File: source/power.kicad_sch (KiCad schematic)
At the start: 105 parts, among them Q1 MMBT5401, Q10 MMBT5401, Q11 CSD19536KCS, Q12 CSD19536KCS, Q2 MMBT5401, Q3 CSD19536KCS, Q4 CSD19536KCS, Q5 MMBT5401, Q6 MMBT5401, Q7 CSD19536KCS, Q8 CSD19536KCS, Q9 MMBT5401, U10 MS8311, U8 MS8311, U9 MS8311

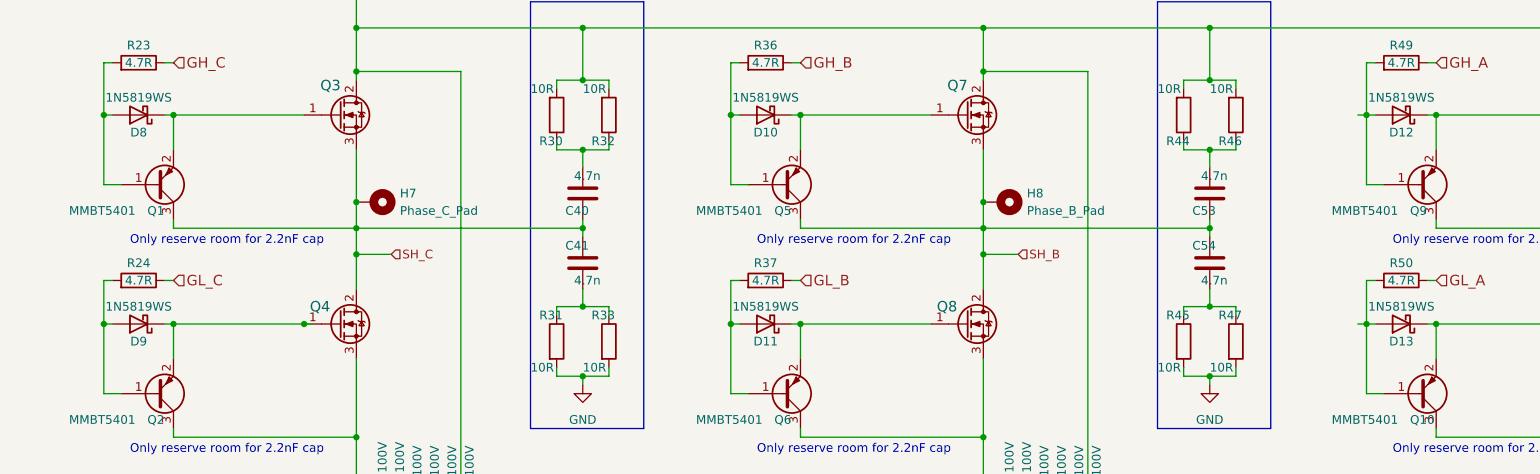
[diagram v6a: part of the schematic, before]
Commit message: Add files via upload
2 missing gnd connections on mcu
missing gnd connection on 12V power supply
pin4 pulled to gnd on 5V power supply
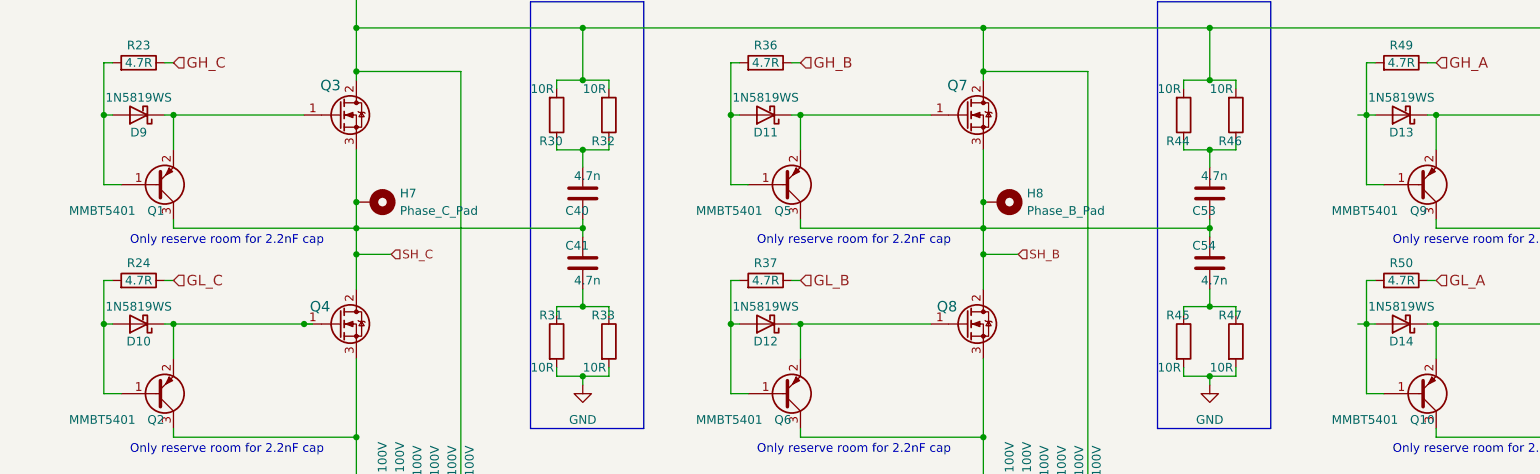
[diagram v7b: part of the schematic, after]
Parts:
- renumbered D9 to D10, D10 to D11, D11 to D12, D12 to D13, D13 to D14, D8 to D9
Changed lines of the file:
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@@
   (symbol (lib_id "Device:D_Schottky") (at 224.79 49.53 180) (unit 1)
     (in_bom yes) (on_board yes)
-    (property "Reference" "D12" (id 0) (at 224.79 52.07 0))
+    (property "Reference" "D13" (id 0) (at 224.79 52.07 0))
     (property "Value" "1N5819WS" (id 1) (at 224.79 46.99 0))
     (property "Footprint" "Diode_SMD:D_SOD-323" (id 2) (at 224.79 49.53 0)
@@
   (symbol (lib_id "Device:D_Schottky") (at 132.08 49.53 180) (unit 1)
     (in_bom yes) (on_board yes)
-    (property "Reference" "D10" (id 0) (at 132.08 52.07 0))
+    (property "Reference" "D11" (id 0) (at 132.08 52.07 0))
     (property "Value" "1N5819WS" (id 1) (at 132.08 46.99 0))
     (property "Footprint" "Diode_SMD:D_SOD-323" (id 2) (at 132.08 49.53 0)
@@
   (symbol (lib_id "Device:D_Schottky") (at 224.79 80.01 180) (unit 1)
     (in_bom yes) (on_board yes)
-    (property "Reference" "D13" (id 0) (at 224.79 82.55 0))
+    (property "Reference" "D14" (id 0) (at 224.79 82.55 0))
     (property "Value" "1N5819WS" (id 1) (at 224.79 77.47 0))
     (property "Footprint" "Diode_SMD:D_SOD-323" (id 2) (at 224.79 80.01 0)
@@
   (symbol (lib_id "Device:D_Schottky") (at 132.08 80.01 180) (unit 1)
     (in_bom yes) (on_board yes)
-    (property "Reference" "D11" (id 0) (at 132.08 82.55 0))
+    (property "Reference" "D12" (id 0) (at 132.08 82.55 0))
     (property "Value" "1N5819WS" (id 1) (at 132.08 77.47 0))
     (property "Footprint" "Diode_SMD:D_SOD-323" (id 2) (at 132.08 80.01 0)
@@
   (symbol (lib_id "Device:D_Schottky") (at 40.64 49.53 180) (unit 1)
     (in_bom yes) (on_board yes)
-    (property "Reference" "D8" (id 0) (at 40.64 52.07 0))
+    (property "Reference" "D9" (id 0) (at 40.64 52.07 0))
     (property "Value" "1N5819WS" (id 1) (at 40.64 46.99 0))
     (property "Footprint" "Diode_SMD:D_SOD-323" (id 2) (at 40.64 49.53 0)
@@
   (symbol (lib_id "Device:D_Schottky") (at 40.64 80.01 180) (unit 1)
     (in_bom yes) (on_board yes)
-    (property "Reference" "D9" (id 0) (at 40.64 82.55 0))
+    (property "Reference" "D10" (id 0) (at 40.64 82.55 0))
     (property "Value" "1N5819WS" (id 1) (at 40.64 77.47 0))
     (property "Footprint" "Diode_SMD:D_SOD-323" (id 2) (at 40.64 80.01 0)

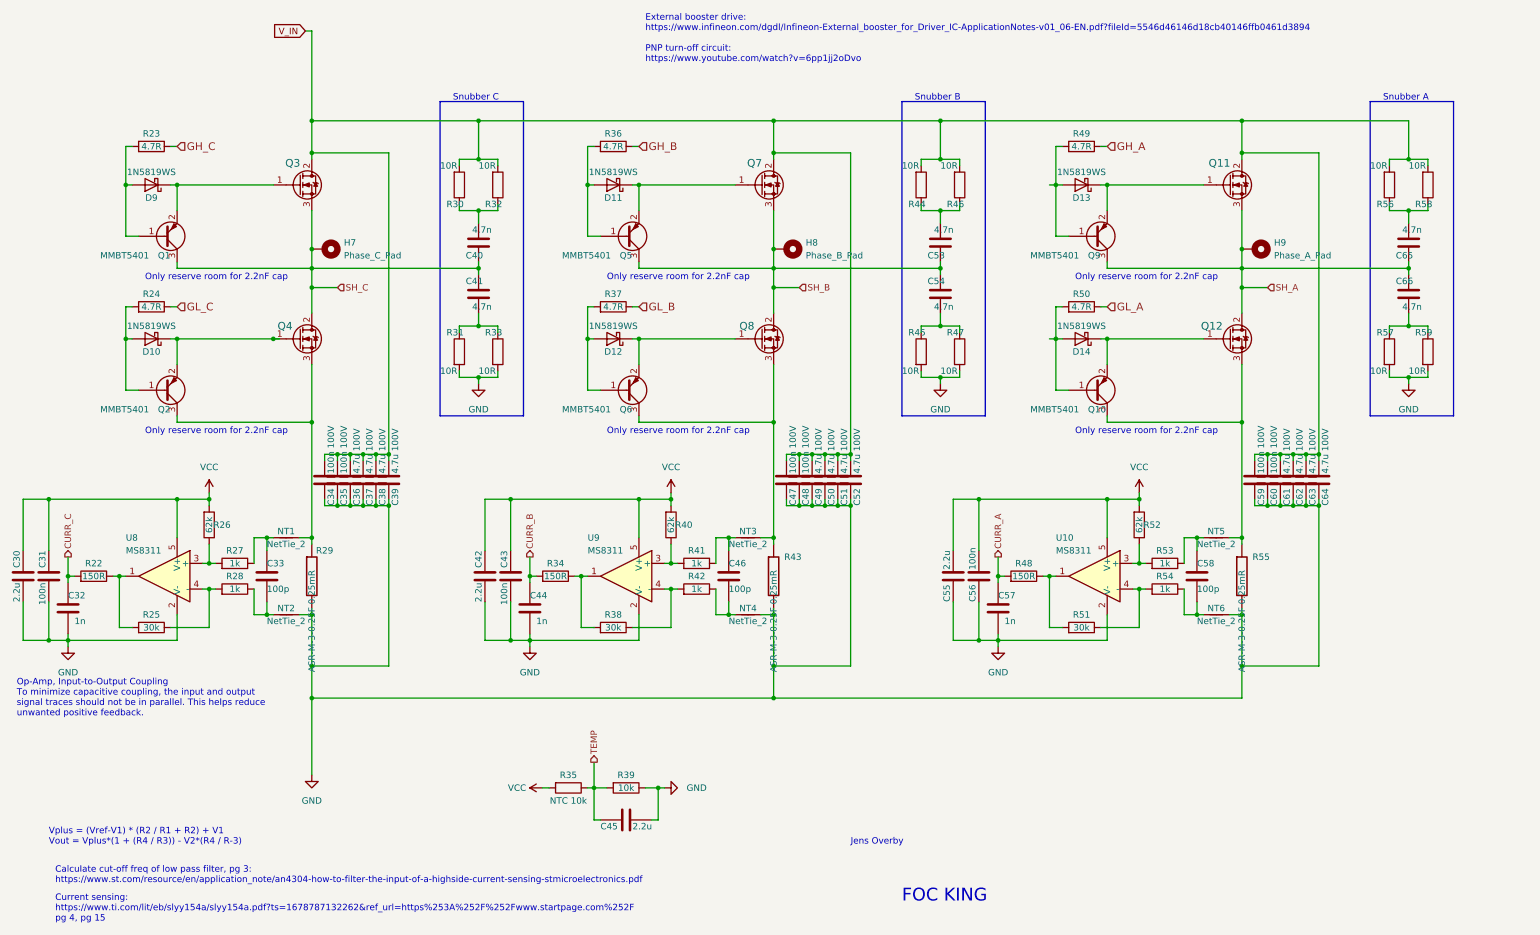
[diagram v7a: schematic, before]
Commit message: JLCPCB order with separate power supply
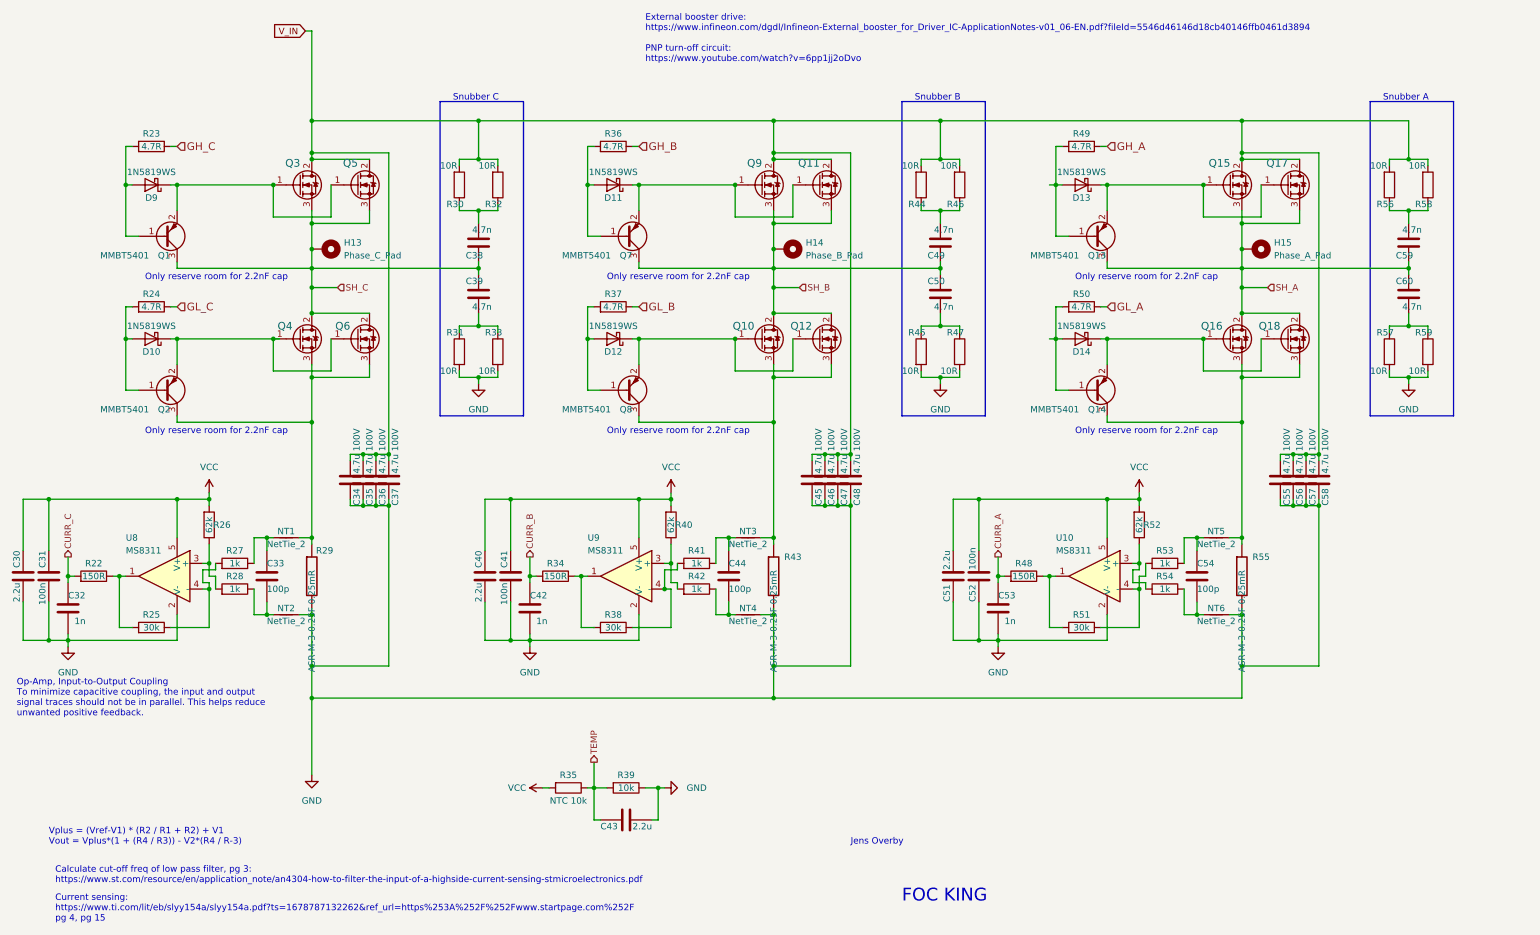
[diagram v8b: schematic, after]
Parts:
- removed C34, C35, C47, C48, C59, C60: 100n 100V, Capacitor_SMD:C_0805_2012Metric, symbol Device:C
- added Q11, Q12, Q17, Q18, Q5, Q6: CSD19536KCS, Custom:TO-220-3_Vertical_bend, symbol Device:Q_NMOS_GDS
- renumbered C36 to C34, C37 to C35, C38 to C36, C39 to C37, C40 to C38, C41 to C39, C42 to C40, C43 to C41, C44 to C42, C45 to C43, C46 to C44, C49 to C45, C50 to C46, C51 to C47, C52 to C48, C53 to C49, C54 to C50, C55 to C51, C56 to C52, C57 to C53, C58 to C54, C61 to C55, C62 to C56, C63 to C57, C64 to C58, C65 to C59, C66 to C60, H7 to H13, H8 to H14, H9 to H15, NT2 to NT1, NT1 to NT2, NT6 to NT5, NT5 to NT6, Q8 to Q10, Q9 to Q13, Q10 to Q14, Q11 to Q15, Q12 to Q16, Q5 to Q7, Q6 to Q8, Q7 to Q9
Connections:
- net GND: now also NT2.2, NT6.2; no longer NT1.2, NT5.2
- net SH_A: now also Q17.3 (S), Q18.2 (D)
- net SH_B: now also Q11.3 (S), Q12.2 (D)
- net SH_C: now also Q5.3 (S), Q6.2 (D)
- net V_IN: now also Q11.2 (D), Q17.2 (D), Q5.2 (D)
- net at C33.2, R27.1: now also NT1.1; no longer NT2.1
- net at R26.1, U8.3 (+): now also R28.2; no longer R27.2
- net at R25.1, U8.4 (-): now also R27.2; no longer R28.2
- net at C54.2, R53.1: now also NT5.1; no longer NT6.1
- net at Q14.3 (C), Q16.3 (S), R55.1: now also NT5.2, Q18.3 (S); no longer NT6.2
- net at NT3.2, Q10.3 (S), Q8.3 (C)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: now also Q12.3 (S)
- net at R40.1, U9.3 (+): now also R42.2; no longer R41.2
- net at C54.1, R54.1: now also NT6.1; no longer NT5.1
- net at R51.1, U10.4 (-): now also R53.2; no longer R54.2
- net at Q2.3 (C), Q4.3 (S), R29.1: now also NT1.2, Q6.3 (S); no longer NT2.2
- net at D12.1 (K), Q10.1 (G), Q8.2 (E): now also Q12.1 (G)
- net at D13.1 (K), Q13.2 (E), Q15.1 (G): now also Q17.1 (G)
- net at D11.1 (K), Q7.2 (E), Q9.1 (G): now also Q11.1 (G)
- net at R38.1, U9.4 (-): now also R41.2; no longer R42.2
- net at C33.1, R28.1: now also NT2.1; no longer NT1.1
- net at D9.1 (K), Q1.2 (E), Q3.1 (G): now also Q5.1 (G)
- net at R52.1, U10.3 (+): now also R54.2; no longer R53.2
- net at D10.1 (K), Q2.2 (E), Q4.1 (G): now also Q6.1 (G)
- net at D14.1 (K), Q14.2 (E), Q16.1 (G): now also Q18.1 (G)
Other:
- moved on the sheet: NT1, NT2, NT5, NT6
